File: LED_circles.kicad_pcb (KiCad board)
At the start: 2 copper layers, 125 x 125 mm, 135 parts, among them J1 Conn_ARM_SWD_EDGE, J2 USB_C_Receptacle, U3 FT230XS, U74 BD33GA3WEFJ, U75 M95256-WMN6P, U76 M95256-WMN6P, U77 STM32G071KBTxN

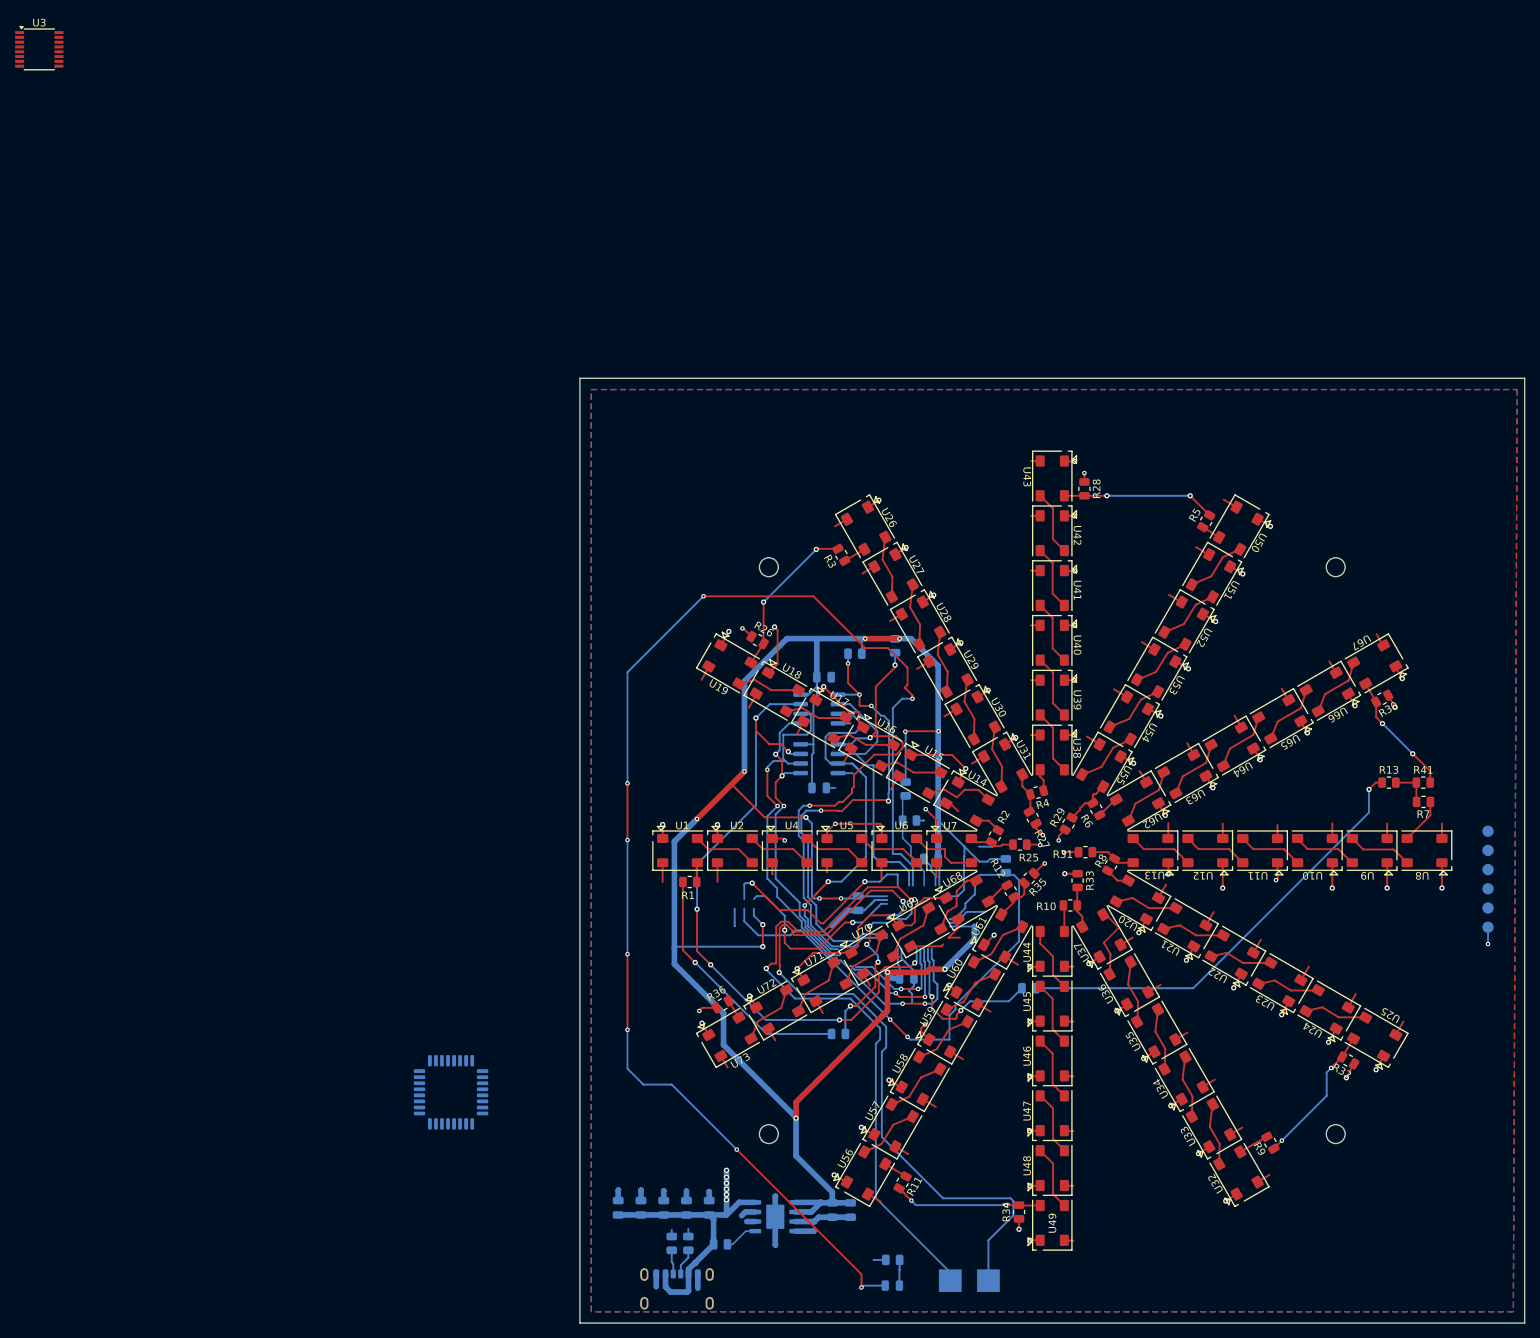
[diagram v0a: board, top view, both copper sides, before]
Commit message: reverted back to power only USB
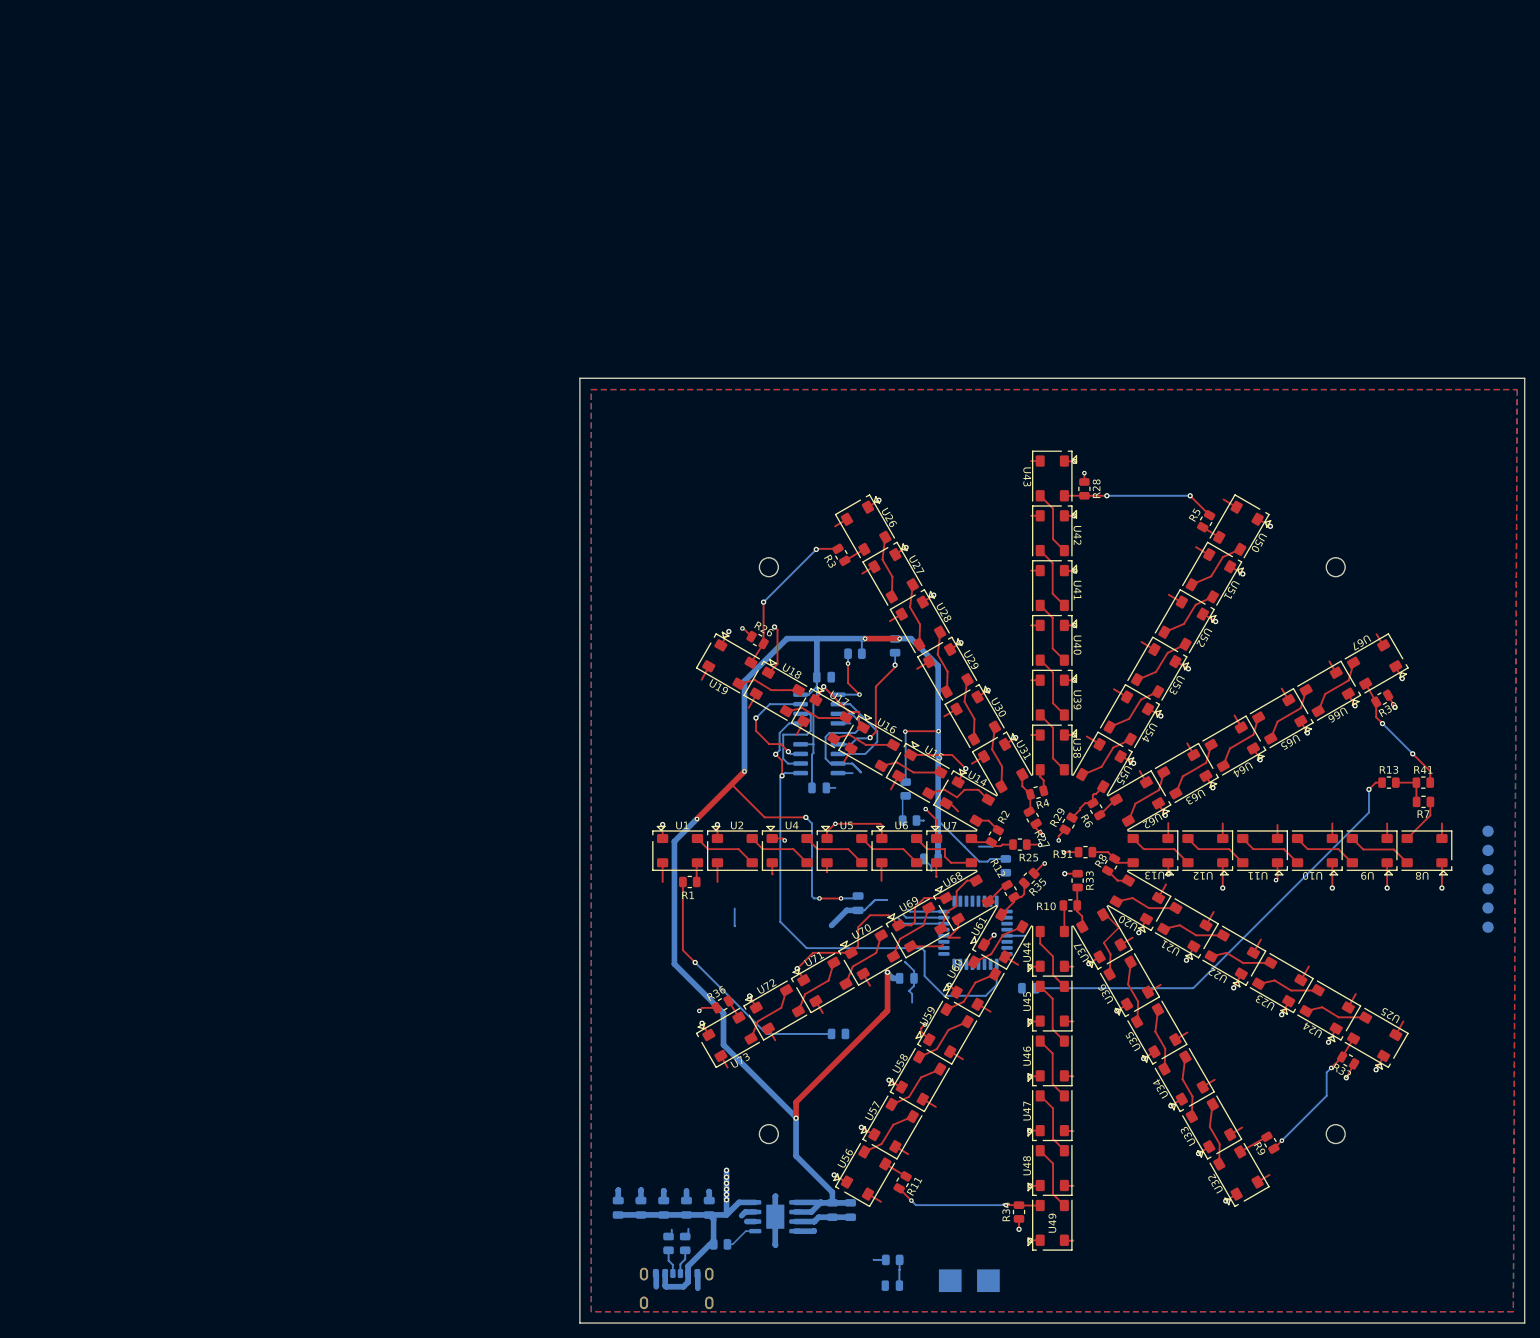
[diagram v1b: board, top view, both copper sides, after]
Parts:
- removed U3: FT230XS, Package_SO:SSOP-16_3.9x4.9mm_P0.635mm
- J2: value USB_C_Receptacle -> USB4125-GF-A
- moved U77 72.5 mm to (133.3, 110.9)
- moved R43 0.42 mm to (92.7, 152.0)
- moved R44 0.42 mm to (94.9, 152.0)
- moved J2 0.07 mm to (93.8, 159.0)
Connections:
- D1 pad 2: unconnected-(D1-A-Pad2) -> Net-(D1-A)
- J2 pad A5: unconnected-(J2-CC1-PadA5) -> Net-(J2-CC1)
- J2 pad A9: Net-(J2-VBUS-PadA4) -> +5V
- J2 pad B5: unconnected-(J2-CC2-PadB5) -> Net-(J2-CC2)
- J2 pad B9: Net-(J2-VBUS-PadA4) -> +5V
- R43 pad 1: unconnected-(R43-Pad1) -> Net-(J2-CC2)
- R44 pad 1: unconnected-(R44-Pad1) -> Net-(J2-CC1)
- U77 pad 1: unconnected-(U77-PB9-Pad1) -> /LED_circles_ucontroller/EEPROM1_CS
- U77 pad 13: unconnected-(U77-PA6-Pad13) -> /LED_circles_ucontroller/SPI1_MISO
- U77 pad 17: unconnected-(U77-PB15-Pad17) -> /LED_circles_ucontroller/EEPROM2_CS
- U77 pad 2: unconnected-(U77-PC14-Pad2) -> /LED_circles_ucontroller/HOLD
- U77 pad 20: unconnected-(U77-PC6-Pad20) -> /LED_circles_ucontroller/WRITE_PROTECT
- U77 pad 32: unconnected-(U77-PB8-Pad32) -> Net-(D1-A)
- U77 pad 6: unconnected-(U77-PF2-Pad6) -> Net-(J1-~{RESET})
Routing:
- net unconnected-(D1-A-Pad2): track 177.7 -> 0.00 mm, vias 8 -> 0
- net unconnected-(TP2-Pad1): track 94.5 -> 0.00 mm, vias 2 -> 0
- net unconnected-(TP1-Pad1): track 90.0 -> 0.00 mm, vias 2 -> 0
- net Net-(J1-~{RESET}): track 74.3 -> 0.00 mm, vias 2 -> 0
- net /LED_circles_ucontroller/HOLD: track 88.8 -> 15.5 mm, vias 6 -> 2
- net +3.3V: track 317.6 -> 260.5 mm, vias 15 -> 11
- net /LED_circles_ucontroller/SPI1_SCK: track 69.4 -> 13.1 mm, vias 4 -> 0
- net /LED_circles_ucontroller/EEPROM2_CS: track 64.0 -> 8.89 mm, vias 5 -> 2
- net /LED_circles_ucontroller/EEPROM1_CS: track 68.6 -> 17.2 mm, vias 3 -> 2
- net /LED_circles_ucontroller/WRITE_PROTECT: track 64.8 -> 19.2 mm, vias 4 -> 0
- net /LED_circles_ucontroller/SWCLK-BOOT0: track 28.7 -> 0.00 mm, vias 2 -> 0
- net Net-(U77-PA0): track 22.5 -> 0.00 mm, vias 2 -> 0
- net /LED_circles_ucontroller/SPI1_MISO: track 36.4 -> 13.9 mm
- net /LED_circles_ucontroller/SWDIO: track 25.4 -> 4.87 mm, vias 2 -> 0
- net Net-(U77-PA8): track 19.7 -> 0.00 mm, vias 4 -> 0
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
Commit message: More layout
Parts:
- moved R49 49.9 mm to (169.9, 111.6)
- moved R50 49.9 mm to (170.4, 115.8)
- moved C8 32.2 mm to (149.7, 111.5)
- moved R37 30.6 mm to (166.4, 111.5), turned to 90 degrees
- moved C11 21.9 mm to (146.7, 111.5), turned to -90 degrees
- moved C10 20.2 mm to (143.7, 111.5), turned to -90 degrees
- moved J1 1.35 mm to (199.8, 103.8)
- moved C12 0.75 mm to (113.3, 76.3)
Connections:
- U77 pad 2: /LED_circles_ucontroller/HOLD -> unconnected-(U77-PC14-Pad2)
- U77 pad 21: unconnected-(U77-PA10/UCPD1_DBCC2-Pad21) -> /LED_circles_ucontroller/HOLD
- U77 pad 4: unconnected-(U77-VDD-Pad4) -> +3.3V
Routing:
- net /LED_circles_ucontroller/HOLD: track 15.5 -> 109.8 mm, vias 2 -> 3
- net /LED_circles_ucontroller/SPI1_SCK: track 13.1 -> 87.9 mm
- net Net-(J1-~{RESET}): track 0.00 -> 74.7 mm
- net +3.3V: track 260.5 -> 190.6 mm, vias 11 -> 5
- net /LED_circles_ucontroller/SWDIO: track 4.87 -> 71.3 mm
- net /LED_circles_ucontroller/SPI1_MISO: track 13.9 -> 77.2 mm, vias 0 -> 4
- net /LED_circles_ucontroller/BOTTOM_ROWS: track 58.9 -> 122.0 mm, vias 1 -> 3
- net /LED_circles_ucontroller/SWCLK-BOOT0: track 0.00 -> 61.3 mm
- net Net-(D1-A): track 0.00 -> 49.5 mm
- net /LED_circles_ucontroller/WRITE_PROTECT: track 19.2 -> 53.1 mm, vias 0 -> 2
- net /LED_circles_ucontroller/EEPROM2_CS: track 8.89 -> 39.3 mm
- net /LED_circles_ucontroller/EEPROM1_CS: track 17.2 -> 47.0 mm
- net GND: track 269.5 -> 252.0 mm, vias 78 -> 77
- net Net-(U77-PA0): track 0.00 -> 7.24 mm
- net /LED_circles_ucontroller/SPI1_MOSI: track 69.5 -> 71.8 mm, vias 2 -> 0
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
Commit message: More layout
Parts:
- moved TP2 71.5 mm to (85.1, 105.8), turned to 0 degrees
- moved TP1 64.3 mm to (85.1, 110.8), turned to 0 degrees
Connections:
- TP1 pad 1: unconnected-(TP1-Pad1) -> /LED_circles_ucontroller/TX
- TP2 pad 1: unconnected-(TP2-Pad1) -> /LED_circles_ucontroller/RX
- U77 pad 1: /LED_circles_ucontroller/EEPROM1_CS -> unconnected-(U77-PB9-Pad1)
- U77 pad 17: /LED_circles_ucontroller/EEPROM2_CS -> unconnected-(U77-PB15-Pad17)
- U77 pad 30: unconnected-(U77-PB6-Pad30) -> /LED_circles_ucontroller/EEPROM2_CS
- U77 pad 31: unconnected-(U77-PB7-Pad31) -> /LED_circles_ucontroller/EEPROM1_CS
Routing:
- net Net-(D1-A): track 49.5 -> 106.7 mm
- net +3.3V: track 190.6 -> 246.5 mm, vias 5 -> 6
- net /LED_circles_ucontroller/RX: track 5.51 -> 50.1 mm, vias 0 -> 2
- net /LED_circles_ucontroller/TX: track 6.38 -> 48.7 mm, vias 0 -> 2
- net Net-(U77-PA8): track 0.00 -> 21.9 mm, vias 0 -> 2
- net /LED_circles_ucontroller/EEPROM1_CS: track 47.0 -> 55.5 mm
- net /LED_circles_ucontroller/EEPROM2_CS: track 39.3 -> 46.8 mm
- net GND: track 252.0 -> 245.0 mm
- net /LED_circles_ucontroller/BOTTOM_ROWS: track 122.0 -> 123.4 mm, vias 3 -> 5
- net /LED_circles_ucontroller/HOLD: track 109.8 -> 109.1 mm
- net /LED_circles_ucontroller/WRITE_PROTECT: track 53.1 -> 53.4 mm, vias 2 -> 4
- net Net-(J1-~{RESET}): vias 0 -> 4
- net /LED_circles_ucontroller/SPI1_SCK: vias 0 -> 2
- net /LED_circles_ucontroller/SWDIO: vias 0 -> 2
- net /LED_circles_ucontroller/SWCLK-BOOT0: vias 0 -> 2
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
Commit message: More layout
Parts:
- moved R37 1.80 mm to (167.0, 109.8)
- moved R49 0.50 mm to (169.4, 111.8)
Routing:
- net /LED_circles_ucontroller/SWCLK-BOOT0: track 61.3 -> 11.3 mm
- net /LED_circles_ucontroller/SWDIO: track 71.3 -> 23.1 mm
- net Net-(J1-~{RESET}): track 74.7 -> 34.5 mm
- net +3.3V: track 246.5 -> 283.3 mm
- net GND: track 245.0 -> 243.1 mm
- net +5V: track 176.5 -> 176.0 mm
- net Net-(D1-A): vias 0 -> 2

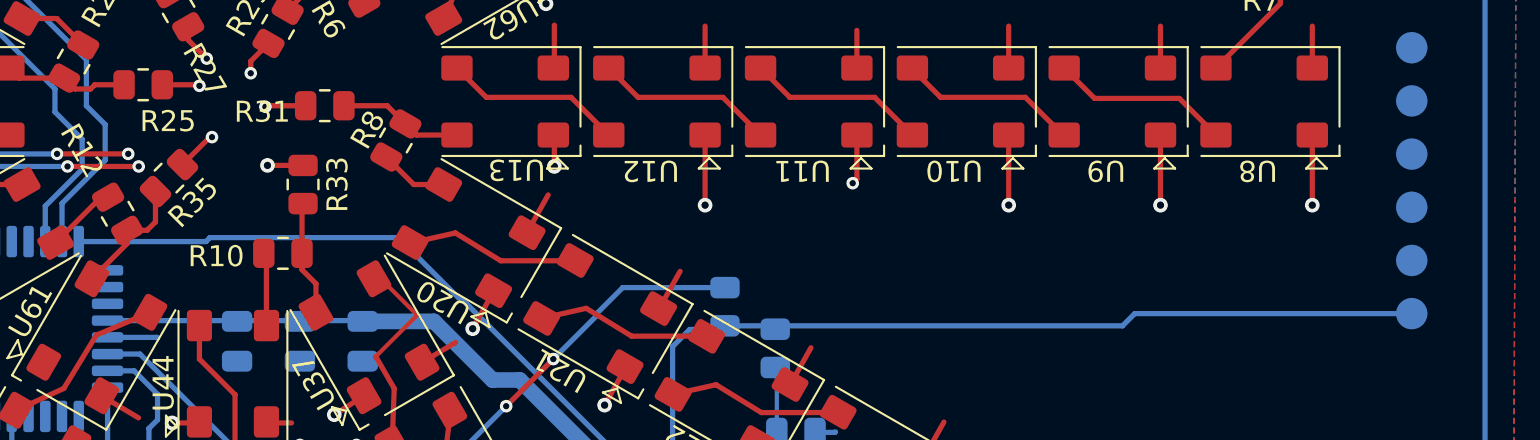
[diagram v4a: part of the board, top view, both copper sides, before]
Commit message: Pin swapping on pogo pins
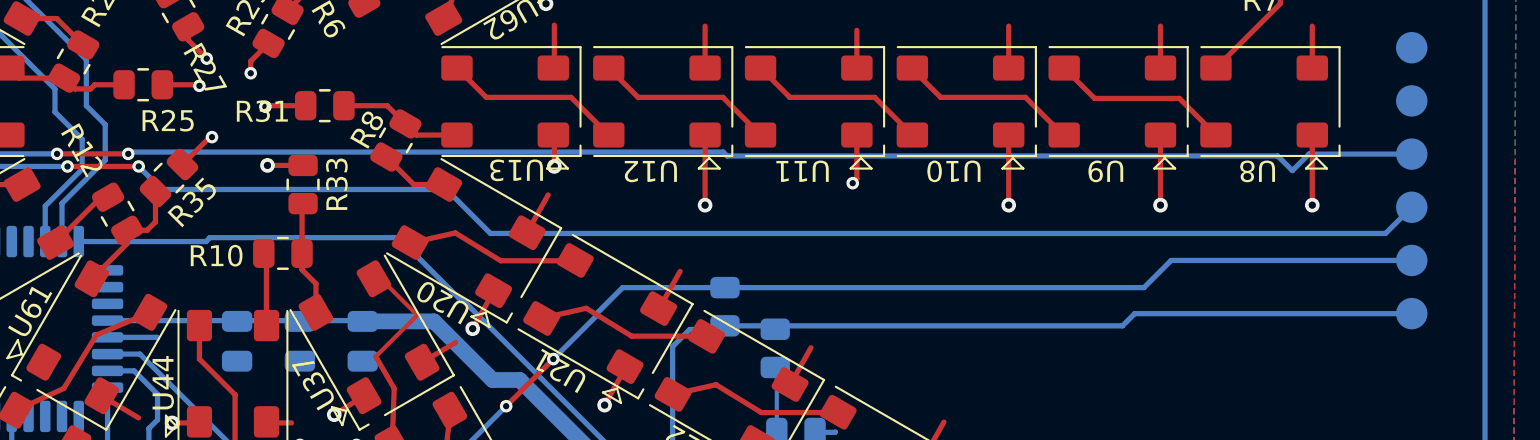
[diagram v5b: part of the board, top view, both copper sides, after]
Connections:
- J1 pad 2: /LED_circles_ucontroller/SWDIO -> Net-(J1-SWDIO)
- J1 pad 3: Net-(J1-~{RESET}) -> /LED_circles_ucontroller/SWCLK-BOOT0
- J1 pad 4: /LED_circles_ucontroller/SWCLK-BOOT0 -> /LED_circles_ucontroller/SWDIO
- R37 pad 2: Net-(J1-~{RESET}) -> Net-(J1-SWDIO)
- U77 pad 6: Net-(J1-~{RESET}) -> Net-(J1-SWDIO)
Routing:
- net Net-(J1-SWDIO): track 0.00 -> 67.8 mm, vias 0 -> 4
- net /LED_circles_ucontroller/SWCLK-BOOT0: track 11.3 -> 74.0 mm
- net /LED_circles_ucontroller/SWDIO: track 23.1 -> 85.1 mm
- net Net-(J1-~{RESET}): track 34.5 -> 0.00 mm, vias 4 -> 0

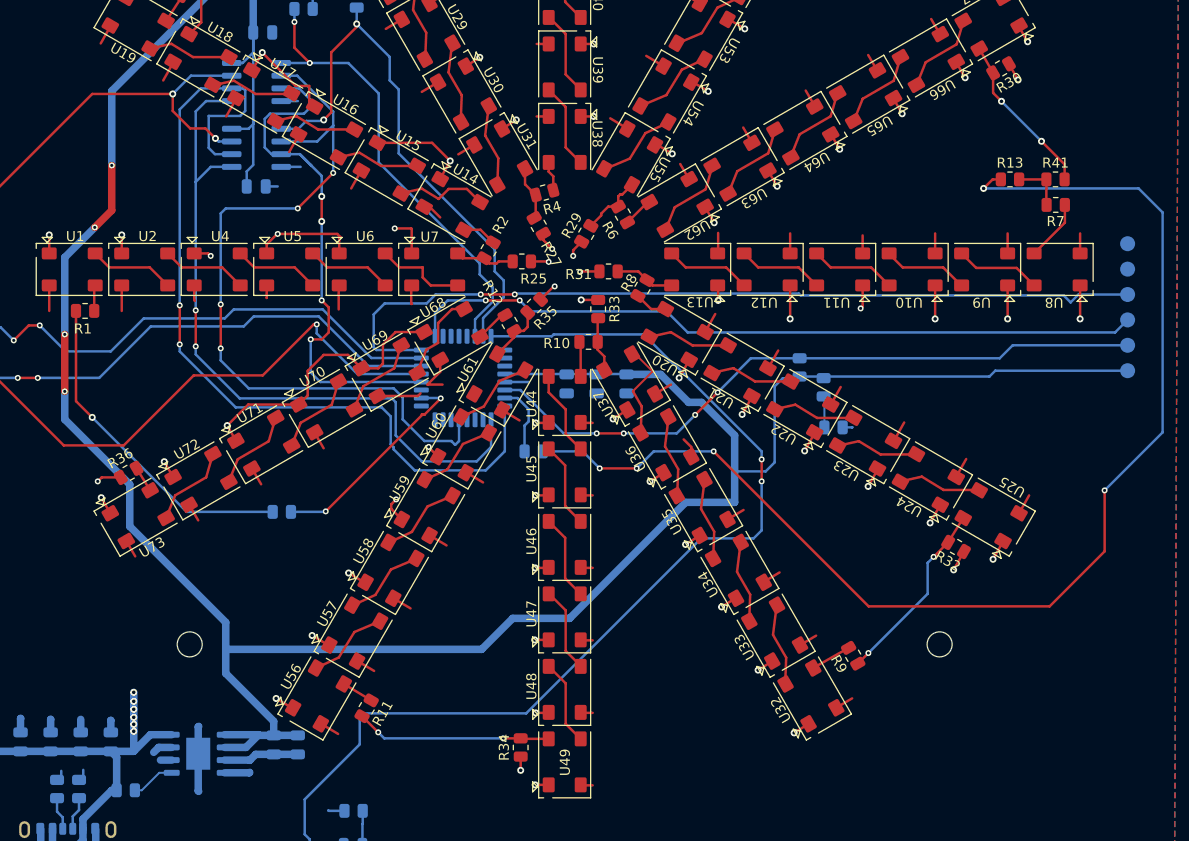
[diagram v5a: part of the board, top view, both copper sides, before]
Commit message: Fixed connectivity problems
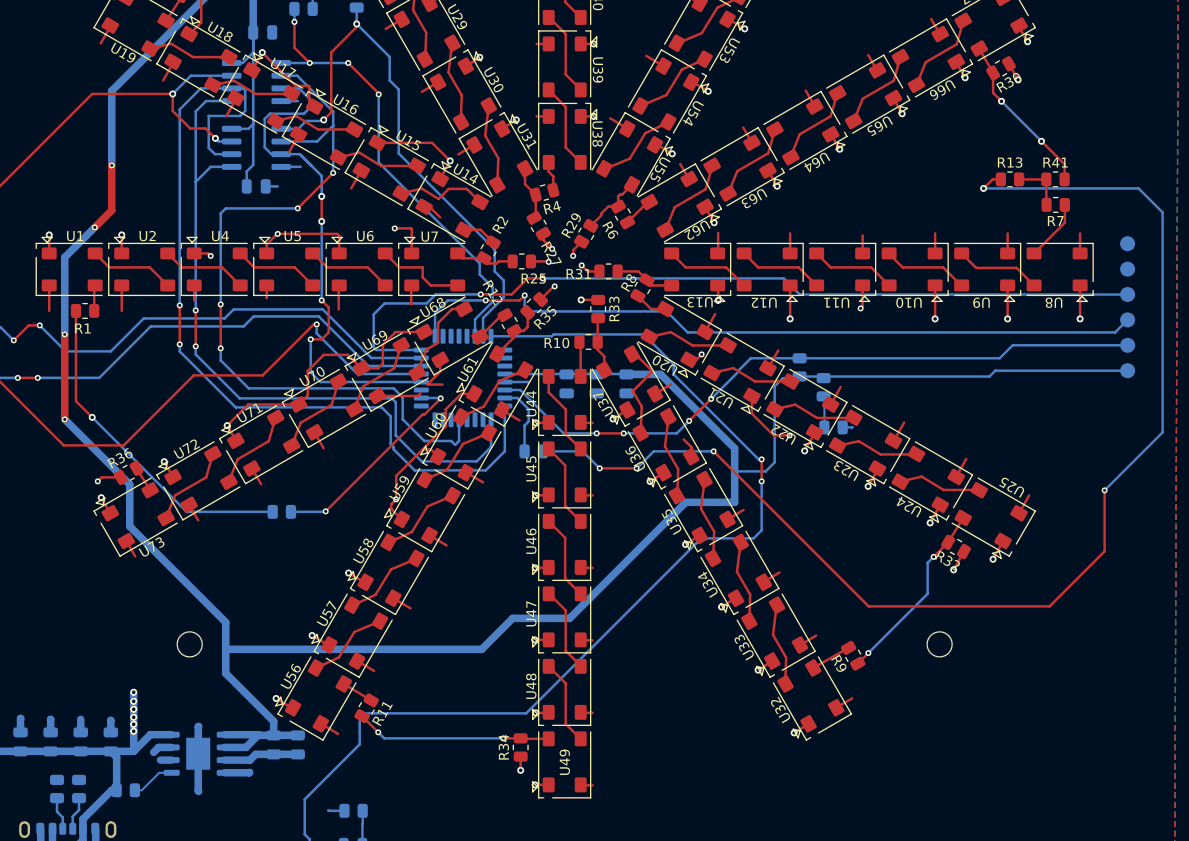
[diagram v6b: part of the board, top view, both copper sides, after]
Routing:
- net GND: track 243.1 -> 260.1 mm, vias 77 -> 76
- net /LED_circles_ucontroller/SWCLK-BOOT0: track 74.0 -> 75.0 mm
- net +3.3V: track 283.3 -> 282.5 mm
- net /LED_circles_ucontroller/SWDIO: track 85.1 -> 85.7 mm
- net /LED_circles_ucontroller/EEPROM2_CS: vias 2 -> 4
